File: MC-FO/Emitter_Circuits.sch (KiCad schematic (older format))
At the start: 8 parts

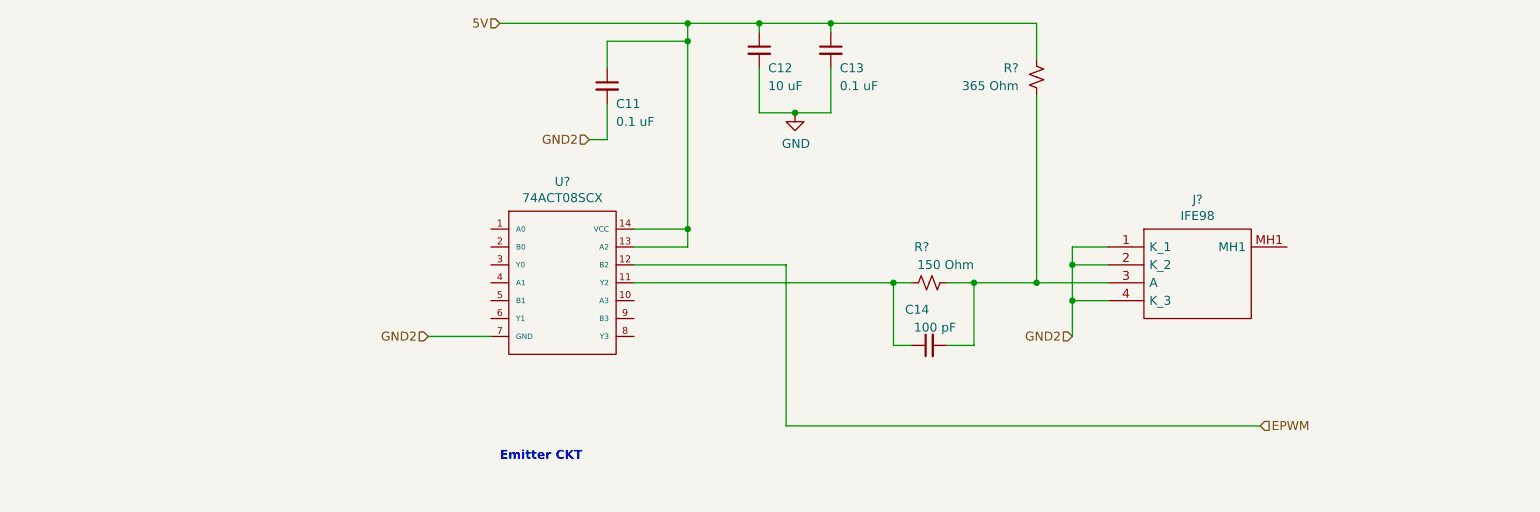
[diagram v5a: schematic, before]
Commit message: Updated naming, Pi filters
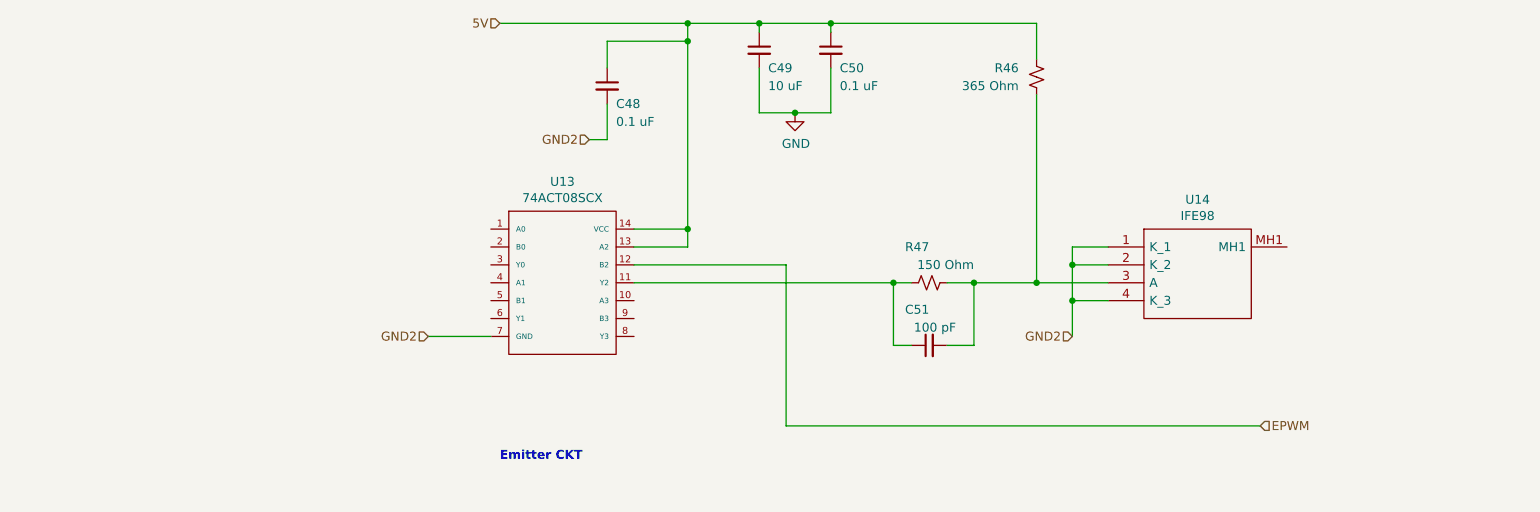
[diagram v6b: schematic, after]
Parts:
- gave numbers to parts that had none: 4
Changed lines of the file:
@@
 $Descr A4 11693 8268
 encoding utf-8
-Sheet 5 11
+Sheet 4 11
 Title ""
 Date ""
@@
 Emitter CKT
 $Comp
-L IFE98:IFE98 J?
+L IFE98:IFE98 U4
 U 1 1 61710D71
 P 7700 4250
-AR Path="/61717EAF/61710D71" Ref="J?"  Part="1"
-AR Path="/617509F7/61710D71" Ref="J?"  Part="1"
-AR Path="/61750A2A/61710D71" Ref="J?"  Part="1"
-AR Path="/6176CA10/61710D71" Ref="J?"  Part="1"
-AR Path="/6176CA81/61710D71" Ref="J?"  Part="1"
-AR Path="/6176CAE4/61710D71" Ref="J?"  Part="1"
-F 0 "J?" H 8200 4515 50  0000 C CNN
+AR Path="/61717EAF/61710D71" Ref="U4"  Part="1"
+AR Path="/617509F7/61710D71" Ref="U6"  Part="1"
+AR Path="/61750A2A/61710D71" Ref="U8"  Part="1"
+AR Path="/6176CA10/61710D71" Ref="U10"  Part="1"
+AR Path="/6176CA81/61710D71" Ref="U12"  Part="1"
+AR Path="/6176CAE4/61710D71" Ref="U14"  Part="1"
+AR Path="/61710D71" Ref="J?"  Part="1"
+F 0 "U14" H 8200 4515 50  0000 C CNN
 F 1 "IFE98" H 8200 4424 50  0000 C CNN
 F 2 "IFE98" H 8550 4350 50  0001 L CNN
@@
 $EndComp
 $Comp
-L Device:R_Small_US R?
+L Device:R_Small_US R20
 U 1 1 617428A7
 P 6700 4450
-AR Path="/61717EAF/617428A7" Ref="R?"  Part="1"
-AR Path="/617509F7/617428A7" Ref="R?"  Part="1"
-AR Path="/61750A2A/617428A7" Ref="R?"  Part="1"
-AR Path="/6176CA10/617428A7" Ref="R?"  Part="1"
-AR Path="/6176CA81/617428A7" Ref="R?"  Part="1"
-AR Path="/6176CAE4/617428A7" Ref="R?"  Part="1"
-F 0 "R?" V 6900 4450 50  0000 L CNN
+AR Path="/61717EAF/617428A7" Ref="R20"  Part="1"
+AR Path="/617509F7/617428A7" Ref="R26"  Part="1"
+AR Path="/61750A2A/617428A7" Ref="R32"  Part="1"
+AR Path="/6176CA10/617428A7" Ref="R37"  Part="1"
+AR Path="/6176CA81/617428A7" Ref="R42"  Part="1"
+AR Path="/6176CAE4/617428A7" Ref="R47"  Part="1"
+F 0 "R47" V 6900 4450 50  0000 L CNN
 F 1 "150 Ohm" V 6800 4200 50  0000 L CNN
 F 2 "" H 6700 4450 50  0001 C CNN
@@
 P 6700 4800
 AR Path="/61717EAF/61748E58" Ref="C14"  Part="1"
-AR Path="/617509F7/61748E58" Ref="C24"  Part="1"
-AR Path="/61750A2A/61748E58" Ref="C?"  Part="1"
-AR Path="/6176CA10/61748E58" Ref="C?"  Part="1"
-AR Path="/6176CA81/61748E58" Ref="C?"  Part="1"
-AR Path="/6176CAE4/61748E58" Ref="C?"  Part="1"
-F 0 "C14" V 6900 4800 50  0000 L CNN
+AR Path="/617509F7/61748E58" Ref="C20"  Part="1"
+AR Path="/61750A2A/61748E58" Ref="C31"  Part="1"
+AR Path="/6176CA10/61748E58" Ref="C38"  Part="1"
+AR Path="/6176CA81/61748E58" Ref="C44"  Part="1"
+AR Path="/6176CAE4/61748E58" Ref="C51"  Part="1"
+F 0 "C51" V 6900 4800 50  0000 L CNN
 F 1 "100 pF" V 6800 4650 50  0000 L CNN
 F 2 "" H 6700 4800 50  0001 C CNN
@@
 	6950 4450 6800 4450
 $Comp
-L Device:R_Small_US R?
+L Device:R_Small_US R21
 U 1 1 6174EB5A
 P 7300 3300
-AR Path="/61717EAF/6174EB5A" Ref="R?"  Part="1"
-AR Path="/617509F7/6174EB5A" Ref="R?"  Part="1"
-AR Path="/61750A2A/6174EB5A" Ref="R?"  Part="1"
-AR Path="/6176CA10/6174EB5A" Ref="R?"  Part="1"
-AR Path="/6176CA81/6174EB5A" Ref="R?"  Part="1"
-AR Path="/6176CAE4/6174EB5A" Ref="R?"  Part="1"
-F 0 "R?" H 7400 3250 50  0000 L CNN
+AR Path="/61717EAF/6174EB5A" Ref="R21"  Part="1"
+AR Path="/617509F7/6174EB5A" Ref="R25"  Part="1"
+AR Path="/61750A2A/6174EB5A" Ref="R31"  Part="1"
+AR Path="/6176CA10/6174EB5A" Ref="R36"  Part="1"
+AR Path="/6176CA81/6174EB5A" Ref="R41"  Part="1"
+AR Path="/6176CAE4/6174EB5A" Ref="R46"  Part="1"
+F 0 "R46" H 7400 3250 50  0000 L CNN
 F 1 "365 Ohm" H 7400 3350 50  0000 L CNN
 F 2 "" H 7300 3300 50  0001 C CNN
@@
 P 4900 3350
 AR Path="/61717EAF/6171F0C9" Ref="C11"  Part="1"
-AR Path="/617509F7/6171F0C9" Ref="C21"  Part="1"
-AR Path="/61750A2A/6171F0C9" Ref="C?"  Part="1"
-AR Path="/6176CA10/6171F0C9" Ref="C?"  Part="1"
-AR Path="/6176CA81/6171F0C9" Ref="C?"  Part="1"
-AR Path="/6176CAE4/6171F0C9" Ref="C?"  Part="1"
-F 0 "C11" H 4950 3250 50  0000 L CNN
+AR Path="/617509F7/6171F0C9" Ref="C17"  Part="1"
+AR Path="/61750A2A/6171F0C9" Ref="C28"  Part="1"
+AR Path="/6176CA10/6171F0C9" Ref="C35"  Part="1"
+AR Path="/6176CA81/6171F0C9" Ref="C41"  Part="1"
+AR Path="/6176CAE4/6171F0C9" Ref="C48"  Part="1"
+F 0 "C48" H 4950 3250 50  0000 L CNN
 F 1 "0.1 uF" H 4950 3150 50  0000 L CNN
 F 2 "" H 4900 3350 50  0001 C CNN
@@
 P 6150 3150
 AR Path="/61717EAF/61733718" Ref="C13"  Part="1"
-AR Path="/617509F7/61733718" Ref="C23"  Part="1"
-AR Path="/61750A2A/61733718" Ref="C?"  Part="1"
-AR Path="/6176CA10/61733718" Ref="C?"  Part="1"
-AR Path="/6176CA81/61733718" Ref="C?"  Part="1"
-AR Path="/6176CAE4/61733718" Ref="C?"  Part="1"
-F 0 "C13" H 6200 3050 50  0000 L CNN
+AR Path="/617509F7/61733718" Ref="C19"  Part="1"
+AR Path="/61750A2A/61733718" Ref="C30"  Part="1"
+AR Path="/6176CA10/61733718" Ref="C37"  Part="1"
+AR Path="/6176CA81/61733718" Ref="C43"  Part="1"
+AR Path="/6176CAE4/61733718" Ref="C50"  Part="1"
+F 0 "C50" H 6200 3050 50  0000 L CNN
 F 1 "0.1 uF" H 6200 2950 50  0000 L CNN
 F 2 "" H 6150 3150 50  0001 C CNN
@@
 P 5750 3150
 AR Path="/61717EAF/61730A88" Ref="C12"  Part="1"
-AR Path="/617509F7/61730A88" Ref="C22"  Part="1"
-AR Path="/61750A2A/61730A88" Ref="C?"  Part="1"
-AR Path="/6176CA10/61730A88" Ref="C?"  Part="1"
-AR Path="/6176CA81/61730A88" Ref="C?"  Part="1"
-AR Path="/6176CAE4/61730A88" Ref="C?"  Part="1"
-F 0 "C12" H 5800 3050 50  0000 L CNN
+AR Path="/617509F7/61730A88" Ref="C18"  Part="1"
+AR Path="/61750A2A/61730A88" Ref="C29"  Part="1"
+AR Path="/6176CA10/61730A88" Ref="C36"  Part="1"
+AR Path="/6176CA81/61730A88" Ref="C42"  Part="1"
+AR Path="/6176CAE4/61730A88" Ref="C49"  Part="1"
+F 0 "C49" H 5800 3050 50  0000 L CNN
 F 1 "10 uF" H 5800 2950 50  0000 L CNN
 F 2 "" H 5750 3150 50  0001 C CNN
@@
 	3900 4750 4250 4750
 $Comp
-L Existing_IC_Models:74ACT08SCX U?
+L Existing_IC_Models:74ACT08SCX U3
 U 1 1 61804FDE
 P 4650 4000
-F 0 "U?" H 4650 4115 50  0000 C CNN
+AR Path="/61717EAF/61804FDE" Ref="U3"  Part="1"
+AR Path="/617509F7/61804FDE" Ref="U5"  Part="1"
+AR Path="/61750A2A/61804FDE" Ref="U7"  Part="1"
+AR Path="/6176CA10/61804FDE" Ref="U9"  Part="1"
+AR Path="/6176CA81/61804FDE" Ref="U11"  Part="1"
+AR Path="/6176CAE4/61804FDE" Ref="U13"  Part="1"
+F 0 "U13" H 4650 4115 50  0000 C CNN
 F 1 "74ACT08SCX" H 4650 4024 50  0000 C CNN
 F 2 "" H 4650 4000 50  0001 C CNN

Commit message: Updated LED Ckts, Added new IC model
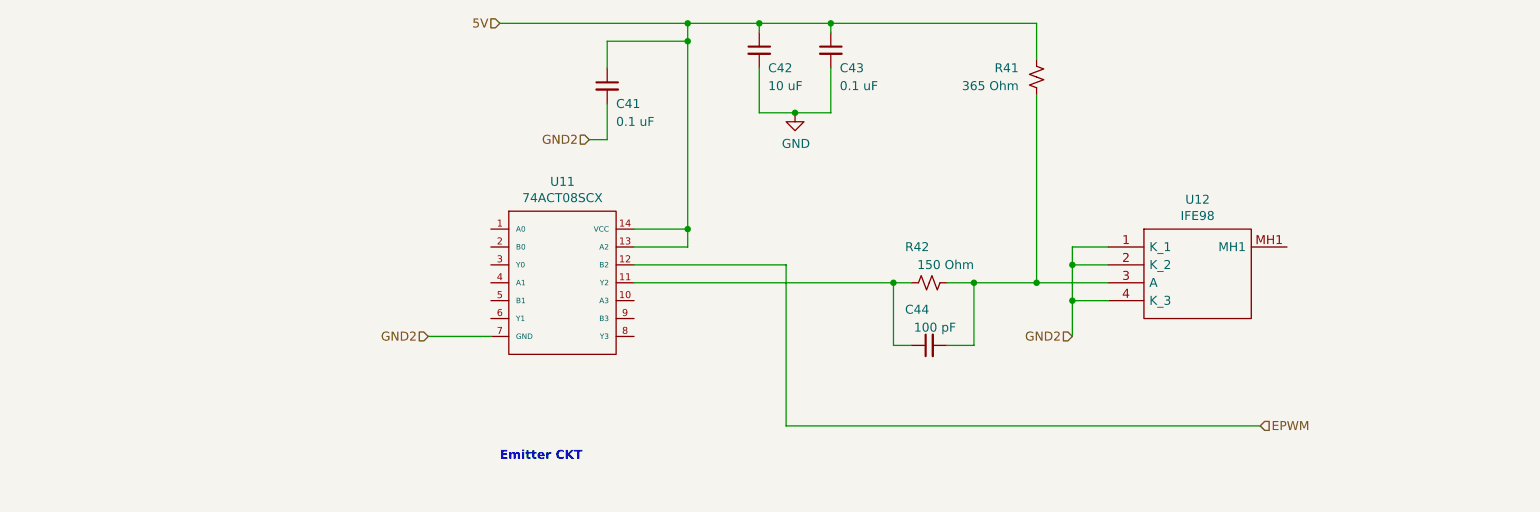
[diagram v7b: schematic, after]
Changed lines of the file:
@@
 $Descr A4 11693 8268
 encoding utf-8
-Sheet 4 11
+Sheet 3 11
 Title ""
 Date ""
@@
 AR Path="/6176CAE4/61710D71" Ref="U14"  Part="1"
 AR Path="/61710D71" Ref="J?"  Part="1"
-F 0 "U14" H 8200 4515 50  0000 C CNN
+F 0 "U12" H 8200 4515 50  0000 C CNN
 F 1 "IFE98" H 8200 4424 50  0000 C CNN
 F 2 "IFE98" H 8550 4350 50  0001 L CNN
@@
 AR Path="/6176CA81/617428A7" Ref="R42"  Part="1"
 AR Path="/6176CAE4/617428A7" Ref="R47"  Part="1"
-F 0 "R47" V 6900 4450 50  0000 L CNN
+F 0 "R42" V 6900 4450 50  0000 L CNN
 F 1 "150 Ohm" V 6800 4200 50  0000 L CNN
 F 2 "" H 6700 4450 50  0001 C CNN
@@
 AR Path="/6176CA81/61748E58" Ref="C44"  Part="1"
 AR Path="/6176CAE4/61748E58" Ref="C51"  Part="1"
-F 0 "C51" V 6900 4800 50  0000 L CNN
+F 0 "C44" V 6900 4800 50  0000 L CNN
 F 1 "100 pF" V 6800 4650 50  0000 L CNN
 F 2 "" H 6700 4800 50  0001 C CNN
@@
 AR Path="/6176CA81/6174EB5A" Ref="R41"  Part="1"
 AR Path="/6176CAE4/6174EB5A" Ref="R46"  Part="1"
-F 0 "R46" H 7400 3250 50  0000 L CNN
+F 0 "R41" H 7400 3250 50  0000 L CNN
 F 1 "365 Ohm" H 7400 3350 50  0000 L CNN
 F 2 "" H 7300 3300 50  0001 C CNN
@@
 AR Path="/6176CA81/6171F0C9" Ref="C41"  Part="1"
 AR Path="/6176CAE4/6171F0C9" Ref="C48"  Part="1"
-F 0 "C48" H 4950 3250 50  0000 L CNN
+F 0 "C41" H 4950 3250 50  0000 L CNN
 F 1 "0.1 uF" H 4950 3150 50  0000 L CNN
 F 2 "" H 4900 3350 50  0001 C CNN
@@
 AR Path="/6176CA81/61733718" Ref="C43"  Part="1"
 AR Path="/6176CAE4/61733718" Ref="C50"  Part="1"
-F 0 "C50" H 6200 3050 50  0000 L CNN
+F 0 "C43" H 6200 3050 50  0000 L CNN
 F 1 "0.1 uF" H 6200 2950 50  0000 L CNN
 F 2 "" H 6150 3150 50  0001 C CNN
@@
 AR Path="/6176CA81/61730A88" Ref="C42"  Part="1"
 AR Path="/6176CAE4/61730A88" Ref="C49"  Part="1"
-F 0 "C49" H 5800 3050 50  0000 L CNN
+F 0 "C42" H 5800 3050 50  0000 L CNN
 F 1 "10 uF" H 5800 2950 50  0000 L CNN
 F 2 "" H 5750 3150 50  0001 C CNN
@@
 AR Path="/6176CA81/61804FDE" Ref="U11"  Part="1"
 AR Path="/6176CAE4/61804FDE" Ref="U13"  Part="1"
-F 0 "U13" H 4650 4115 50  0000 C CNN
+F 0 "U11" H 4650 4115 50  0000 C CNN
 F 1 "74ACT08SCX" H 4650 4024 50  0000 C CNN
 F 2 "" H 4650 4000 50  0001 C CNN

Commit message: Add files via upload
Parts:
- removed R21: 365 Ohm, symbol Device:R_Small_US
- removed U4: IFE98, IFE98, symbol IFE98:IFE98
- added R8: 365 Ohm, symbol Device:R_Small_US
- added U8: IFE98, symbol Existing_IC_Models:IFE98
- renumbered C11 to C13, C12 to C14, C13 to C15, C14 to C16, R20 to R7, U3 to U7
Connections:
- net 5V: now also R8.2
- net GND2: now also U8.1 (K_1), U8.2 (K_2), U8.4 (K_3)
- net at C16.2, R7.2: now also R8.1, U8.3 (A)
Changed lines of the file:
@@
 $Descr A4 11693 8268
 encoding utf-8
-Sheet 3 11
+Sheet 5 11
 Title ""
 Date ""
@@
 Emitter CKT
 $Comp
-L IFE98:IFE98 U4
-U 1 1 61710D71
-P 7700 4250
-AR Path="/61717EAF/61710D71" Ref="U4"  Part="1"
-AR Path="/617509F7/61710D71" Ref="U6"  Part="1"
-AR Path="/61750A2A/61710D71" Ref="U8"  Part="1"
-AR Path="/6176CA10/61710D71" Ref="U10"  Part="1"
-AR Path="/6176CA81/61710D71" Ref="U12"  Part="1"
-AR Path="/6176CAE4/61710D71" Ref="U14"  Part="1"
-AR Path="/61710D71" Ref="J?"  Part="1"
-F 0 "U12" H 8200 4515 50  0000 C CNN
-F 1 "IFE98" H 8200 4424 50  0000 C CNN
-F 2 "IFE98" H 8550 4350 50  0001 L CNN
-F 3 "https://i-fiberoptics.com/pdf/ife98-2-20.pdf" H 8550 4250 50  0001 L CNN
-F 4 "LED FIBER OPTIC 50MBPS 650NM RED RoHS : Compliant" H 8550 4150 50  0001 L CNN "Description"
-F 5 "8.705" H 8550 4050 50  0001 L CNN "Height"
-F 6 "Industrial Fiberoptics" H 8550 3950 50  0001 L CNN "Manufacturer_Name"
-F 7 "IFE98" H 8550 3850 50  0001 L CNN "Manufacturer_Part_Number"
-F 8 "" H 8550 3750 50  0001 L CNN "Mouser Part Number"
-F 9 "" H 8550 3650 50  0001 L CNN "Mouser Price/Stock"
-F 10 "" H 8550 3550 50  0001 L CNN "Arrow Part Number"
-F 11 "" H 8550 3450 50  0001 L CNN "Arrow Price/Stock"
-	1    7700 4250
-	1    0    0    -1
-$EndComp
-$Comp
-L Device:R_Small_US R20
+L Device:R_Small_US R7
 U 1 1 617428A7
 P 6700 4450
-AR Path="/61717EAF/617428A7" Ref="R20"  Part="1"
-AR Path="/617509F7/617428A7" Ref="R26"  Part="1"
-AR Path="/61750A2A/617428A7" Ref="R32"  Part="1"
-AR Path="/6176CA10/617428A7" Ref="R37"  Part="1"
-AR Path="/6176CA81/617428A7" Ref="R42"  Part="1"
-AR Path="/6176CAE4/617428A7" Ref="R47"  Part="1"
-F 0 "R42" V 6900 4450 50  0000 L CNN
+AR Path="/61717EAF/617428A7" Ref="R7"  Part="1"
+AR Path="/617509F7/617428A7" Ref="R9"  Part="1"
+AR Path="/61750A2A/617428A7" Ref="R11"  Part="1"
+AR Path="/6176CA10/617428A7" Ref="R1"  Part="1"
+AR Path="/6176CA81/617428A7" Ref="R3"  Part="1"
+AR Path="/6176CAE4/617428A7" Ref="R5"  Part="1"
+F 0 "R7" V 6900 4450 50  0000 L CNN
 F 1 "150 Ohm" V 6800 4200 50  0000 L CNN
 F 2 "" H 6700 4450 50  0001 C CNN
@@
 $EndComp
 $Comp
-L Device:C_Small C14
+L Device:C_Small C16
 U 1 1 61748E58
 P 6700 4800
-AR Path="/61717EAF/61748E58" Ref="C14"  Part="1"
+AR Path="/61717EAF/61748E58" Ref="C16"  Part="1"
 AR Path="/617509F7/61748E58" Ref="C20"  Part="1"
-AR Path="/61750A2A/61748E58" Ref="C31"  Part="1"
-AR Path="/6176CA10/61748E58" Ref="C38"  Part="1"
-AR Path="/6176CA81/61748E58" Ref="C44"  Part="1"
-AR Path="/6176CAE4/61748E58" Ref="C51"  Part="1"
-F 0 "C44" V 6900 4800 50  0000 L CNN
+AR Path="/61750A2A/61748E58" Ref="C24"  Part="1"
+AR Path="/6176CA10/61748E58" Ref="C4"  Part="1"
+AR Path="/6176CA81/61748E58" Ref="C8"  Part="1"
+AR Path="/6176CAE4/61748E58" Ref="C12"  Part="1"
+F 0 "C16" V 6900 4800 50  0000 L CNN
 F 1 "100 pF" V 6800 4650 50  0000 L CNN
 F 2 "" H 6700 4800 50  0001 C CNN
@@
 	6950 4450 6800 4450
 $Comp
-L Device:R_Small_US R21
-U 1 1 6174EB5A
+L Device:R_Small_US R8
+U 1 1 6178E7F7
 P 7300 3300
-AR Path="/61717EAF/6174EB5A" Ref="R21"  Part="1"
-AR Path="/617509F7/6174EB5A" Ref="R25"  Part="1"
-AR Path="/61750A2A/6174EB5A" Ref="R31"  Part="1"
-AR Path="/6176CA10/6174EB5A" Ref="R36"  Part="1"
-AR Path="/6176CA81/6174EB5A" Ref="R41"  Part="1"
-AR Path="/6176CAE4/6174EB5A" Ref="R46"  Part="1"
-F 0 "R41" H 7400 3250 50  0000 L CNN
+AR Path="/61717EAF/6178E7F7" Ref="R8"  Part="1"
+AR Path="/617509F7/6178E7F7" Ref="R10"  Part="1"
+AR Path="/61750A2A/6178E7F7" Ref="R12"  Part="1"
+AR Path="/6176CA10/6178E7F7" Ref="R2"  Part="1"
+AR Path="/6176CA81/6178E7F7" Ref="R4"  Part="1"
+AR Path="/6176CAE4/6178E7F7" Ref="R6"  Part="1"
+F 0 "R8" H 7400 3250 50  0000 L CNN
 F 1 "365 Ohm" H 7400 3350 50  0000 L CNN
 F 2 "" H 7300 3300 50  0001 C CNN
@@
 	4900 3100 4900 3250
 $Comp
-L Device:C_Small C11
+L Device:C_Small C13
 U 1 1 6171F0C9
 P 4900 3350
-AR Path="/61717EAF/6171F0C9" Ref="C11"  Part="1"
+AR Path="/61717EAF/6171F0C9" Ref="C13"  Part="1"
 AR Path="/617509F7/6171F0C9" Ref="C17"  Part="1"
-AR Path="/61750A2A/6171F0C9" Ref="C28"  Part="1"
-AR Path="/6176CA10/6171F0C9" Ref="C35"  Part="1"
-AR Path="/6176CA81/6171F0C9" Ref="C41"  Part="1"
-AR Path="/6176CAE4/6171F0C9" Ref="C48"  Part="1"
-F 0 "C41" H 4950 3250 50  0000 L CNN
+AR Path="/61750A2A/6171F0C9" Ref="C21"  Part="1"
+AR Path="/6176CA10/6171F0C9" Ref="C1"  Part="1"
+AR Path="/6176CA81/6171F0C9" Ref="C5"  Part="1"
+AR Path="/6176CAE4/6171F0C9" Ref="C9"  Part="1"
+F 0 "C13" H 4950 3250 50  0000 L CNN
 F 1 "0.1 uF" H 4950 3150 50  0000 L CNN
 F 2 "" H 4900 3350 50  0001 C CNN
@@
 	5950 3500 5750 3500
 $Comp
-L power:GND #PWR?
+L power:GND #PWR04
 U 1 1 61735A2B
 P 5950 3500
-AR Path="/61717EAF/61735A2B" Ref="#PWR?"  Part="1"
-AR Path="/617509F7/61735A2B" Ref="#PWR?"  Part="1"
-AR Path="/61750A2A/61735A2B" Ref="#PWR?"  Part="1"
-AR Path="/6176CA10/61735A2B" Ref="#PWR?"  Part="1"
-AR Path="/6176CA81/61735A2B" Ref="#PWR?"  Part="1"
-AR Path="/6176CAE4/61735A2B" Ref="#PWR?"  Part="1"
-F 0 "#PWR?" H 5950 3250 50  0001 C CNN
+AR Path="/61717EAF/61735A2B" Ref="#PWR04"  Part="1"
+AR Path="/617509F7/61735A2B" Ref="#PWR05"  Part="1"
+AR Path="/61750A2A/61735A2B" Ref="#PWR06"  Part="1"
+AR Path="/6176CA10/61735A2B" Ref="#PWR01"  Part="1"
+AR Path="/6176CA81/61735A2B" Ref="#PWR02"  Part="1"
+AR Path="/6176CAE4/61735A2B" Ref="#PWR03"  Part="1"
+F 0 "#PWR04" H 5950 3250 50  0001 C CNN
 F 1 "GND" H 5955 3327 50  0000 C CNN
 F 2 "" H 5950 3500 50  0001 C CNN
@@
 $EndComp
 $Comp
-L Device:C_Small C13
+L Device:C_Small C15
 U 1 1 61733718
 P 6150 3150
-AR Path="/61717EAF/61733718" Ref="C13"  Part="1"
+AR Path="/61717EAF/61733718" Ref="C15"  Part="1"
 AR Path="/617509F7/61733718" Ref="C19"  Part="1"
-AR Path="/61750A2A/61733718" Ref="C30"  Part="1"
-AR Path="/6176CA10/61733718" Ref="C37"  Part="1"
-AR Path="/6176CA81/61733718" Ref="C43"  Part="1"
-AR Path="/6176CAE4/61733718" Ref="C50"  Part="1"
-F 0 "C43" H 6200 3050 50  0000 L CNN
+AR Path="/61750A2A/61733718" Ref="C23"  Part="1"
+AR Path="/6176CA10/61733718" Ref="C3"  Part="1"
+AR Path="/6176CA81/61733718" Ref="C7"  Part="1"
+AR Path="/6176CAE4/61733718" Ref="C11"  Part="1"
+F 0 "C15" H 6200 3050 50  0000 L CNN
 F 1 "0.1 uF" H 6200 2950 50  0000 L CNN
 F 2 "" H 6150 3150 50  0001 C CNN
@@
 	5750 3000 5750 3050
 $Comp
-L Device:C_Small C12
+L Device:C_Small C14
 U 1 1 61730A88
 P 5750 3150
-AR Path="/61717EAF/61730A88" Ref="C12"  Part="1"
+AR Path="/61717EAF/61730A88" Ref="C14"  Part="1"
 AR Path="/617509F7/61730A88" Ref="C18"  Part="1"
-AR Path="/61750A2A/61730A88" Ref="C29"  Part="1"
-AR Path="/6176CA10/61730A88" Ref="C36"  Part="1"
-AR Path="/6176CA81/61730A88" Ref="C42"  Part="1"
-AR Path="/6176CAE4/61730A88" Ref="C49"  Part="1"
-F 0 "C42" H 5800 3050 50  0000 L CNN
+AR Path="/61750A2A/61730A88" Ref="C22"  Part="1"
+AR Path="/6176CA10/61730A88" Ref="C2"  Part="1"
+AR Path="/6176CA81/61730A88" Ref="C6"  Part="1"
+AR Path="/6176CAE4/61730A88" Ref="C10"  Part="1"
+F 0 "C14" H 5800 3050 50  0000 L CNN
 F 1 "10 uF" H 5800 2950 50  0000 L CNN
 F 2 "" H 5750 3150 50  0001 C CNN
@@
 	3900 4750 4250 4750
 $Comp
-L Existing_IC_Models:74ACT08SCX U3
+L Existing_IC_Models:74ACT08SCX U7
 U 1 1 61804FDE
 P 4650 4000
-AR Path="/61717EAF/61804FDE" Ref="U3"  Part="1"
-AR Path="/617509F7/61804FDE" Ref="U5"  Part="1"
-AR Path="/61750A2A/61804FDE" Ref="U7"  Part="1"
-AR Path="/6176CA10/61804FDE" Ref="U9"  Part="1"
-AR Path="/6176CA81/61804FDE" Ref="U11"  Part="1"
-AR Path="/6176CAE4/61804FDE" Ref="U13"  Part="1"
-F 0 "U11" H 4650 4115 50  0000 C CNN
+AR Path="/61717EAF/61804FDE" Ref="U7"  Part="1"
+AR Path="/617509F7/61804FDE" Ref="U9"  Part="1"
+AR Path="/61750A2A/61804FDE" Ref="U11"  Part="1"
+AR Path="/6176CA10/61804FDE" Ref="U1"  Part="1"
+AR Path="/6176CA81/61804FDE" Ref="U3"  Part="1"
+AR Path="/6176CAE4/61804FDE" Ref="U5"  Part="1"
+F 0 "U7" H 4650 4115 50  0000 C CNN
 F 1 "74ACT08SCX" H 4650 4024 50  0000 C CNN
 F 2 "" H 4650 4000 50  0001 C CNN
@@
 Wire Wire Line
 	4900 3650 4800 3650
+$Comp
+L Existing_IC_Models:IFE98 U8
+U 1 1 61778B54
+P 8000 4150
+AR Path="/61717EAF/61778B54" Ref="U8"  Part="1"
+AR Path="/61750A2A/61778B54" Ref="U12"  Part="1"
+AR Path="/6176CA10/61778B54" Ref="U2"  Part="1"
+AR Path="/6176CA81/61778B54" Ref="U4"  Part="1"
+AR Path="/6176CAE4/61778B54" Ref="U6"  Part="1"
+AR Path="/617509F7/61778B54" Ref="U10"  Part="1"
+F 0 "U8" H 8000 4265 50  0000 C CNN
+F 1 "IFE98" H 8000 4174 50  0000 C CNN
+F 2 "" H 8000 4150 50  0001 C CNN
+F 3 "" H 8000 4150 50  0001 C CNN
+	1    8000 4150
+	1    0    0    -1
+$EndComp
 $EndSCHEMATC
